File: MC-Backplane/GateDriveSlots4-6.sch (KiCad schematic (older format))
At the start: 3 parts

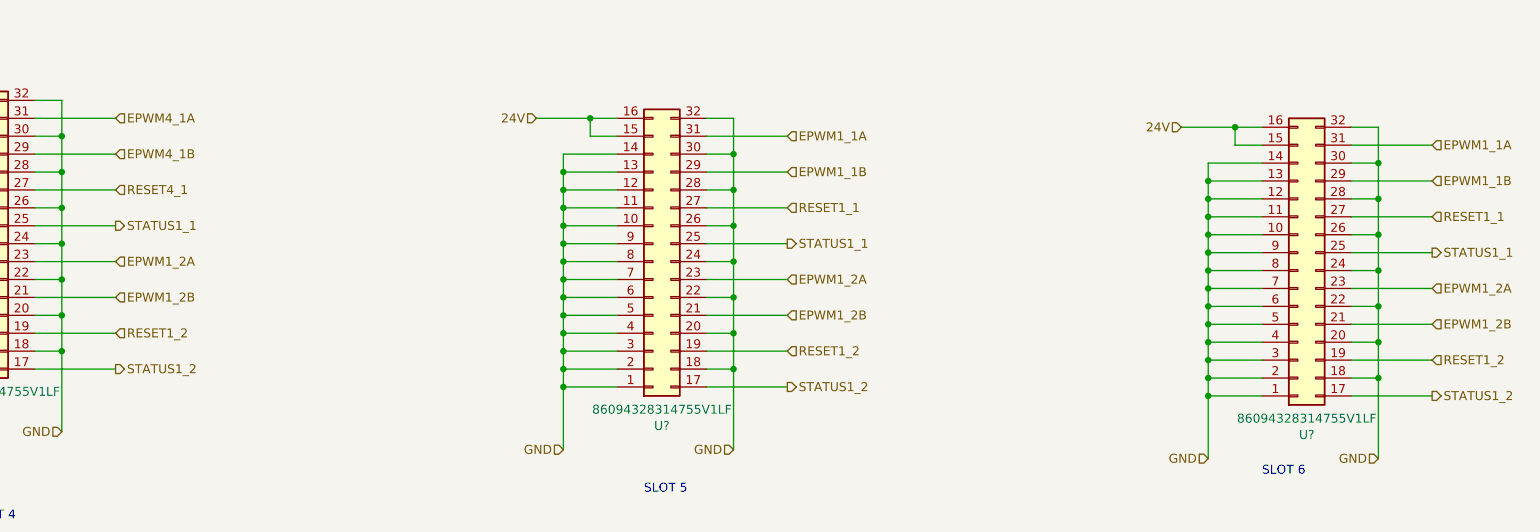
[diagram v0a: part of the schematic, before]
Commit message: added signals for FO slots
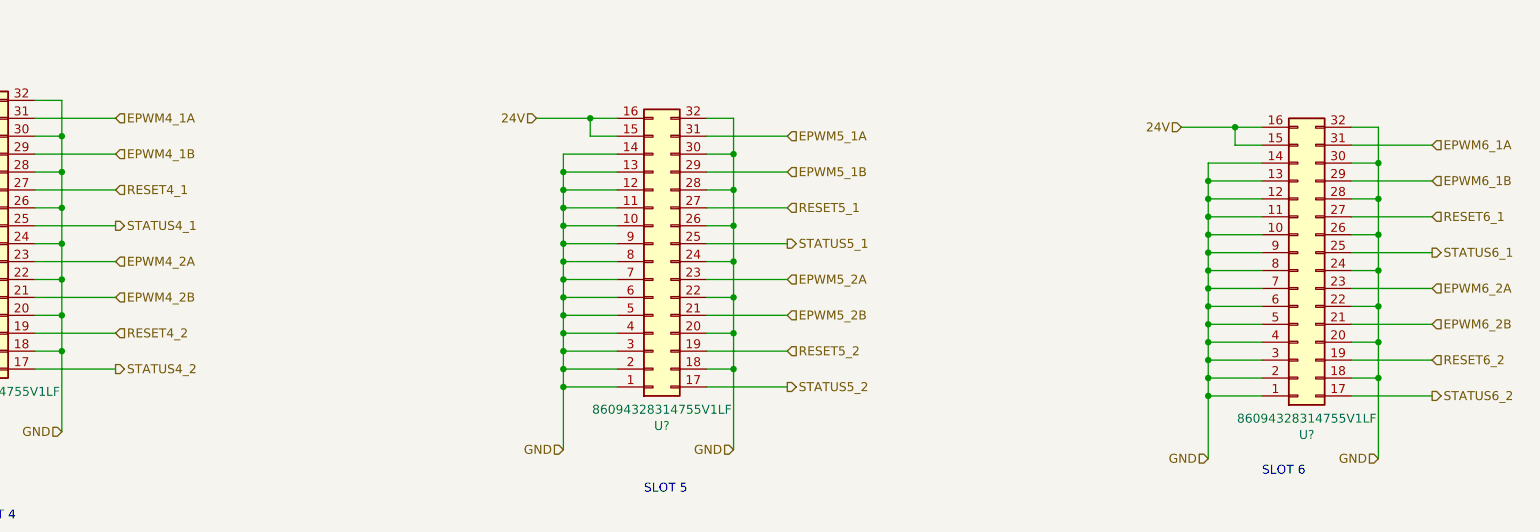
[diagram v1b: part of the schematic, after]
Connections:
- net EPWM1_1A renamed EPWM5_1A
- net EPWM5_1A: no longer U?.31 (Pin_31)
- net EPWM1_1B renamed EPWM5_1B
- net EPWM5_1B: no longer U?.29 (Pin_29)
- removed net EPWM1_2A: U?.23 (Pin_23), U?.23 (Pin_23), U?.23 (Pin_23)
- removed net EPWM1_2B: U?.21 (Pin_21), U?.21 (Pin_21), U?.21 (Pin_21)
- net RESET1_1 renamed RESET5_1
- net RESET5_1: no longer U?.27 (Pin_27)
- removed net RESET1_2: U?.19 (Pin_19), U?.19 (Pin_19), U?.19 (Pin_19)
- removed net STATUS1_1: U?.25 (Pin_25), U?.25 (Pin_25), U?.25 (Pin_25)
- removed net STATUS1_2: U?.17 (Pin_17), U?.17 (Pin_17), U?.17 (Pin_17)
- new net EPWM4_2A: U?.23 (Pin_23)
- new net EPWM4_2B: U?.21 (Pin_21)
- new net EPWM5_2A: U?.23 (Pin_23)
- new net EPWM5_2B: U?.21 (Pin_21)
- new net EPWM6_1A: U?.31 (Pin_31)
- new net EPWM6_1B: U?.29 (Pin_29)
- new net EPWM6_2A: U?.23 (Pin_23)
- new net EPWM6_2B: U?.21 (Pin_21)
- new net RESET4_2: U?.19 (Pin_19)
- new net RESET5_2: U?.19 (Pin_19)
- new net RESET6_1: U?.27 (Pin_27)
- new net RESET6_2: U?.19 (Pin_19)
- new net STATUS4_1: U?.25 (Pin_25)
- new net STATUS4_2: U?.17 (Pin_17)
- new net STATUS5_1: U?.25 (Pin_25)
- new net STATUS5_2: U?.17 (Pin_17)
- new net STATUS6_1: U?.25 (Pin_25)
- new net STATUS6_2: U?.17 (Pin_17)

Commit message: Add files via upload
updating net names and wires
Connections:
- net GND: no longer U?.11 (Pin_11), U?.11 (Pin_11), U?.11 (Pin_11), U?.13 (Pin_13), U?.13 (Pin_13), U?.13 (Pin_13)
- net EPWM4_1A renamed GD_EPWM4_1A
- net EPWM4_1B renamed GD_EPWM4_1B
- net EPWM4_2A renamed GD_EPWM4_2A
- net EPWM4_2B renamed GD_EPWM4_2B
- net EPWM5_1A renamed GD_EPWM5_1A
- net EPWM5_1B renamed GD_EPWM5_1B
- net EPWM5_2A renamed GD_EPWM5_2A
- net EPWM5_2B renamed GD_EPWM5_2B
- net EPWM6_1A renamed GD_EPWM6_1A
- net EPWM6_1B renamed GD_EPWM6_1B
- net EPWM6_2A renamed GD_EPWM6_2A
- net EPWM6_2B renamed GD_EPWM6_2B
- net RESET4_1 renamed GD_RESET4_1
- net RESET4_2 renamed GD_RESET4_2
- net RESET5_1 renamed GD_RESET5_1
- net RESET5_2 renamed GD_RESET5_2
- net RESET6_1 renamed GD_RESET6_1
- net RESET6_2 renamed GD_RESET6_2
- net STATUS4_1 renamed GD_DPWM_STATUS4_1
- net STATUS4_2 renamed GD_DPWM_STATUS4_2
- net STATUS5_1 renamed GD_DPWM_STATUS5_1
- net STATUS5_2 renamed GD_DPWM_STATUS5_2
- net STATUS6_1 renamed GD_DPWM_STATUS6_1
- net STATUS6_2 renamed GD_DPWM_STATUS6_2
- new net EMITTER_ENABLE: U?.13 (Pin_13), U?.13 (Pin_13)
- new net SAFE_STATE_FLAG: U?.11 (Pin_11), U?.11 (Pin_11)
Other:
- note removed: "edit the signal names"
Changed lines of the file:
@@
 $Descr A4 11693 8268
 encoding utf-8
-Sheet 6 7
+Sheet 7 7
 Title ""
 Date ""
@@
 Text Notes 1900 5250 0    50   ~ 0
 SLOT 4
-Text Notes 4650 1300 0    50   ~ 0
-edit the signal names
 $Comp
 L MC-Backplane:86094328314755V1LF U?
@@
 	1750 3100 1450 3100
 Wire Wire Line
-	1450 3100 1450 3200
-Wire Wire Line
-	1750 3200 1450 3200
-Connection ~ 1450 3200
-Wire Wire Line
-	1450 3200 1450 3300
-Wire Wire Line
 	1750 3300 1450 3300
 Connection ~ 1450 3300
-Wire Wire Line
-	1450 3300 1450 3400
-Wire Wire Line
-	1750 3400 1450 3400
-Connection ~ 1450 3400
-Wire Wire Line
-	1450 3400 1450 3500
 Wire Wire Line
 	1750 3500 1450 3500
@@
 GND
 Text HLabel 2700 3000 2    50   Input ~ 0
-EPWM4_1A
+GD_EPWM4_1A
 Wire Wire Line
 	2250 4400 2700 4400
@@
 	2250 4200 2700 4200
 Text HLabel 2700 3200 2    50   Input ~ 0
-EPWM4_1B
+GD_EPWM4_1B
 Text HLabel 2700 3400 2    50   Input ~ 0
-RESET4_1
+GD_RESET4_1
 Text HLabel 2700 3600 2    50   Output ~ 0
-STATUS4_1
+GD_DPWM_STATUS4_1
 Text HLabel 2700 3800 2    50   Input ~ 0
-EPWM4_2A
+GD_EPWM4_2A
 Text HLabel 2700 4000 2    50   Input ~ 0
-EPWM4_2B
+GD_EPWM4_2B
 Text HLabel 2700 4200 2    50   Input ~ 0
-RESET4_2
+GD_RESET4_2
 Text HLabel 2700 4400 2    50   Output ~ 0
-STATUS4_2
+GD_DPWM_STATUS4_2
 Text HLabel 1300 2900 0    50   Input ~ 0
 24V
@@
 24V
 Text HLabel 10050 4550 2    50   Output ~ 0
-STATUS6_2
+GD_DPWM_STATUS6_2
 Text HLabel 10050 4350 2    50   Input ~ 0
-RESET6_2
+GD_RESET6_2
 Text HLabel 10050 4150 2    50   Input ~ 0
-EPWM6_2B
+GD_EPWM6_2B
 Text HLabel 10050 3950 2    50   Input ~ 0
-EPWM6_2A
+GD_EPWM6_2A
 Text HLabel 10050 3750 2    50   Output ~ 0
-STATUS6_1
+GD_DPWM_STATUS6_1
 Text HLabel 10050 3550 2    50   Input ~ 0
-RESET6_1
+GD_RESET6_1
 Text HLabel 10050 3350 2    50   Input ~ 0
-EPWM6_1B
+GD_EPWM6_1B
 Wire Wire Line
 	9600 4350 10050 4350
@@
 	9600 4550 10050 4550
 Text HLabel 10050 3150 2    50   Input ~ 0
-EPWM6_1A
+GD_EPWM6_1A
 Text HLabel 9750 4900 0    50   Input ~ 0
 GND
@@
 Wire Wire Line
 	9100 3650 8800 3650
-Wire Wire Line
-	8800 3550 8800 3650
-Connection ~ 8800 3550
-Wire Wire Line
-	9100 3550 8800 3550
-Wire Wire Line
-	8800 3450 8800 3550
 Connection ~ 8800 3450
 Wire Wire Line
 	9100 3450 8800 3450
-Wire Wire Line
-	8800 3350 8800 3450
-Connection ~ 8800 3350
-Wire Wire Line
-	9100 3350 8800 3350
-Wire Wire Line
-	8800 3250 8800 3350
 Wire Wire Line
 	9100 3250 8800 3250
@@
 24V
 Text HLabel 6450 4500 2    50   Output ~ 0
-STATUS5_2
+GD_DPWM_STATUS5_2
 Text HLabel 6450 4300 2    50   Input ~ 0
-RESET5_2
+GD_RESET5_2
 Text HLabel 6450 4100 2    50   Input ~ 0
-EPWM5_2B
+GD_EPWM5_2B
 Text HLabel 6450 3900 2    50   Input ~ 0
-EPWM5_2A
+GD_EPWM5_2A
 Text HLabel 6450 3700 2    50   Output ~ 0
-STATUS5_1
+GD_DPWM_STATUS5_1
 Text HLabel 6450 3500 2    50   Input ~ 0
-RESET5_1
+GD_RESET5_1
 Text HLabel 6450 3300 2    50   Input ~ 0
-EPWM5_1B
+GD_EPWM5_1B
 Wire Wire Line
 	6000 4300 6450 4300
@@
 	6000 4500 6450 4500
 Text HLabel 6450 3100 2    50   Input ~ 0
-EPWM5_1A
+GD_EPWM5_1A
 Text HLabel 6150 4850 0    50   Input ~ 0
 GND
@@
 Wire Wire Line
 	5500 3600 5200 3600
-Wire Wire Line
-	5200 3500 5200 3600
-Connection ~ 5200 3500
-Wire Wire Line
-	5500 3500 5200 3500
-Wire Wire Line
-	5200 3400 5200 3500
 Connection ~ 5200 3400
 Wire Wire Line
 	5500 3400 5200 3400
-Wire Wire Line
-	5200 3300 5200 3400
-Connection ~ 5200 3300
-Wire Wire Line
-	5500 3300 5200 3300
-Wire Wire Line
-	5200 3200 5200 3300
 Wire Wire Line
 	5500 3200 5200 3200
@@
 Wire Wire Line
 	6000 3100 6450 3100
+Text Notes 9100 5000 0    50   ~ 0
+SLOT 6
+Text Notes 5650 5100 0    50   ~ 0
+SLOT 5
+Wire Wire Line
+	1450 3100 1450 3300
+Wire Wire Line
+	1450 3300 1450 3500
+Wire Wire Line
+	5200 3200 5200 3400
+Wire Wire Line
+	5200 3400 5200 3600
+Wire Wire Line
+	8800 3250 8800 3450
+Wire Wire Line
+	8800 3450 8800 3650
+Text HLabel 1300 3400 0    50   BiDi ~ 0
+SAFE_STATE_FLAG
+Text HLabel 1300 3200 0    50   Input ~ 0
+EMITTER_ENABLE
+Text HLabel 5050 3500 0    50   BiDi ~ 0
+SAFE_STATE_FLAG
+Text HLabel 5050 3300 0    50   Input ~ 0
+EMITTER_ENABLE
+Text HLabel 8650 3550 0    50   BiDi ~ 0
+SAFE_STATE_FLAG
+Text HLabel 8650 3350 0    50   Input ~ 0
+EMITTER_ENABLE
+Wire Wire Line
+	1750 3200 1300 3200
+Wire Wire Line
+	1300 3400 1750 3400
+Wire Wire Line
+	5050 3300 5500 3300
 $Comp
 L MC-Backplane:86094328314755V1LF U?
@@
 	1    0    0    1
 $EndComp
-Text Notes 9100 5000 0    50   ~ 0
-SLOT 6
-Text Notes 5650 5100 0    50   ~ 0
-SLOT 5
+Wire Wire Line
+	5500 3500 5050 3500
 $EndSCHEMATC

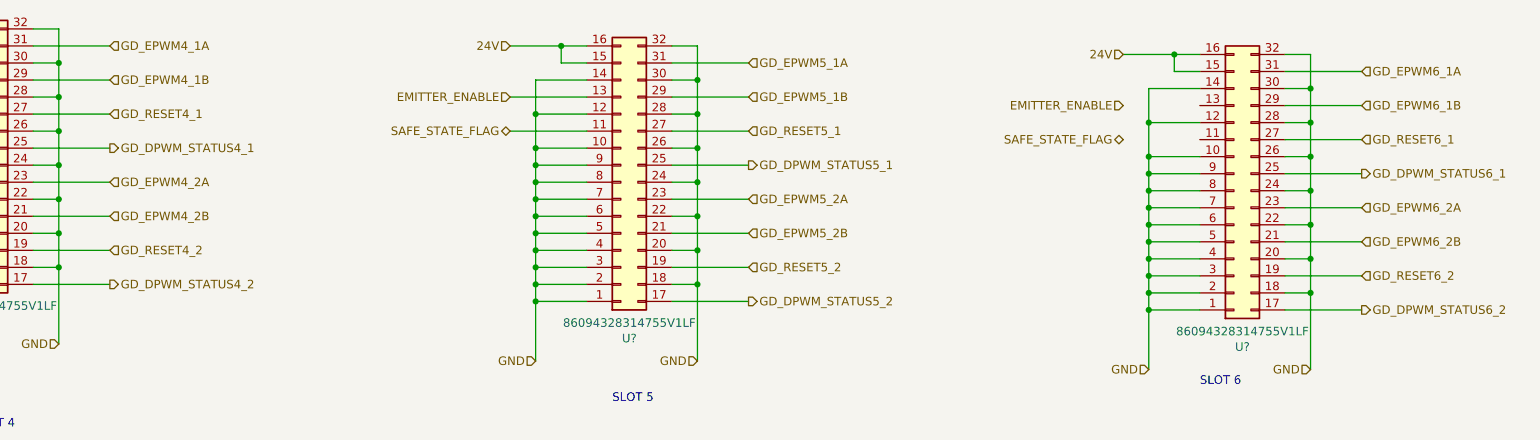
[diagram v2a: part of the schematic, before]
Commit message: Signal naming cleanup/ dsp pin pairing
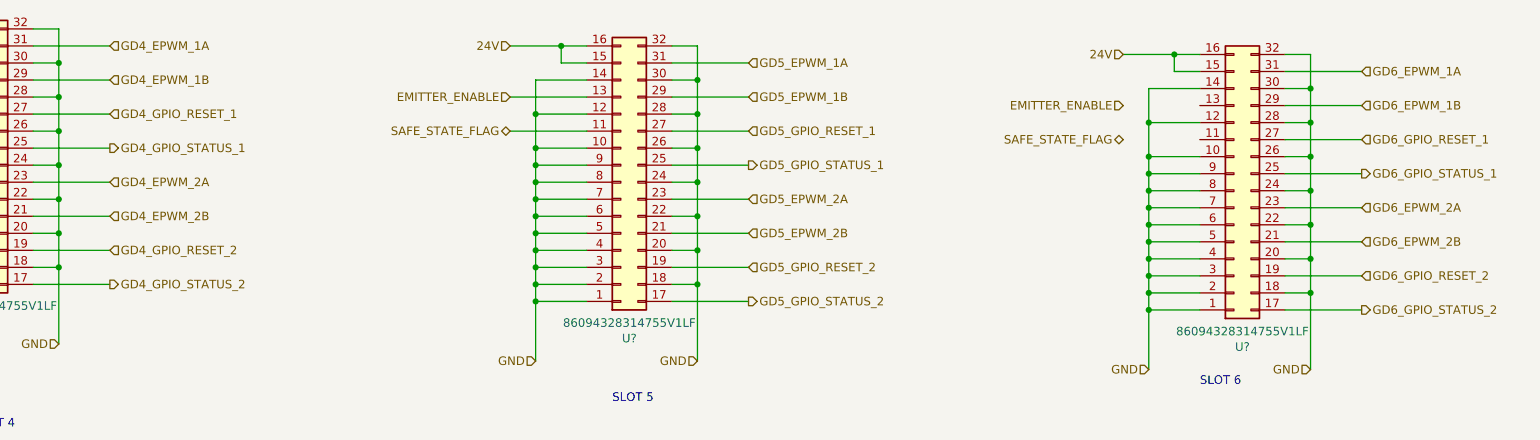
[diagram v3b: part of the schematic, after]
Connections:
- net GD_DPWM_STATUS4_1 renamed GD4_GPIO_STATUS_1
- net GD_DPWM_STATUS4_2 renamed GD4_GPIO_STATUS_2
- net GD_DPWM_STATUS5_1 renamed GD5_GPIO_STATUS_1
- net GD_DPWM_STATUS5_2 renamed GD5_GPIO_STATUS_2
- net GD_DPWM_STATUS6_1 renamed GD6_GPIO_STATUS_1
- net GD_DPWM_STATUS6_2 renamed GD6_GPIO_STATUS_2
- net GD_EPWM4_1A renamed GD4_EPWM_1A
- net GD_EPWM4_1B renamed GD4_EPWM_1B
- net GD_EPWM4_2A renamed GD4_EPWM_2A
- net GD_EPWM4_2B renamed GD4_EPWM_2B
- net GD_EPWM5_1A renamed GD5_EPWM_1A
- net GD_EPWM5_1B renamed GD5_EPWM_1B
- net GD_EPWM5_2A renamed GD5_EPWM_2A
- net GD_EPWM5_2B renamed GD5_EPWM_2B
- net GD_EPWM6_1A renamed GD6_EPWM_1A
- net GD_EPWM6_1B renamed GD6_EPWM_1B
- net GD_EPWM6_2A renamed GD6_EPWM_2A
- net GD_EPWM6_2B renamed GD6_EPWM_2B
- net GD_RESET4_1 renamed GD4_GPIO_RESET_1
- net GD_RESET4_2 renamed GD4_GPIO_RESET_2
- net GD_RESET5_1 renamed GD5_GPIO_RESET_1
- net GD_RESET5_2 renamed GD5_GPIO_RESET_2
- net GD_RESET6_1 renamed GD6_GPIO_RESET_1
- net GD_RESET6_2 renamed GD6_GPIO_RESET_2
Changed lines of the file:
@@
 $Descr A4 11693 8268
 encoding utf-8
-Sheet 7 7
+Sheet 5 7
 Title ""
 Date ""
@@
 GND
 Text HLabel 2700 3000 2    50   Input ~ 0
-GD_EPWM4_1A
+GD4_EPWM_1A
 Wire Wire Line
 	2250 4400 2700 4400
@@
 	2250 4200 2700 4200
 Text HLabel 2700 3200 2    50   Input ~ 0
-GD_EPWM4_1B
+GD4_EPWM_1B
 Text HLabel 2700 3400 2    50   Input ~ 0
-GD_RESET4_1
+GD4_GPIO_RESET_1
 Text HLabel 2700 3600 2    50   Output ~ 0
-GD_DPWM_STATUS4_1
+GD4_GPIO_STATUS_1
 Text HLabel 2700 3800 2    50   Input ~ 0
-GD_EPWM4_2A
+GD4_EPWM_2A
 Text HLabel 2700 4000 2    50   Input ~ 0
-GD_EPWM4_2B
+GD4_EPWM_2B
 Text HLabel 2700 4200 2    50   Input ~ 0
-GD_RESET4_2
+GD4_GPIO_RESET_2
 Text HLabel 2700 4400 2    50   Output ~ 0
-GD_DPWM_STATUS4_2
+GD4_GPIO_STATUS_2
 Text HLabel 1300 2900 0    50   Input ~ 0
 24V
@@
 24V
 Text HLabel 10050 4550 2    50   Output ~ 0
-GD_DPWM_STATUS6_2
+GD6_GPIO_STATUS_2
 Text HLabel 10050 4350 2    50   Input ~ 0
-GD_RESET6_2
+GD6_GPIO_RESET_2
 Text HLabel 10050 4150 2    50   Input ~ 0
-GD_EPWM6_2B
+GD6_EPWM_2B
 Text HLabel 10050 3950 2    50   Input ~ 0
-GD_EPWM6_2A
+GD6_EPWM_2A
 Text HLabel 10050 3750 2    50   Output ~ 0
-GD_DPWM_STATUS6_1
+GD6_GPIO_STATUS_1
 Text HLabel 10050 3550 2    50   Input ~ 0
-GD_RESET6_1
+GD6_GPIO_RESET_1
 Text HLabel 10050 3350 2    50   Input ~ 0
-GD_EPWM6_1B
+GD6_EPWM_1B
 Wire Wire Line
 	9600 4350 10050 4350
@@
 	9600 4550 10050 4550
 Text HLabel 10050 3150 2    50   Input ~ 0
-GD_EPWM6_1A
+GD6_EPWM_1A
 Text HLabel 9750 4900 0    50   Input ~ 0
 GND
@@
 24V
 Text HLabel 6450 4500 2    50   Output ~ 0
-GD_DPWM_STATUS5_2
+GD5_GPIO_STATUS_2
 Text HLabel 6450 4300 2    50   Input ~ 0
-GD_RESET5_2
+GD5_GPIO_RESET_2
 Text HLabel 6450 4100 2    50   Input ~ 0
-GD_EPWM5_2B
+GD5_EPWM_2B
 Text HLabel 6450 3900 2    50   Input ~ 0
-GD_EPWM5_2A
+GD5_EPWM_2A
 Text HLabel 6450 3700 2    50   Output ~ 0
-GD_DPWM_STATUS5_1
+GD5_GPIO_STATUS_1
 Text HLabel 6450 3500 2    50   Input ~ 0
-GD_RESET5_1
+GD5_GPIO_RESET_1
 Text HLabel 6450 3300 2    50   Input ~ 0
-GD_EPWM5_1B
+GD5_EPWM_1B
 Wire Wire Line
 	6000 4300 6450 4300
@@
 	6000 4500 6450 4500
 Text HLabel 6450 3100 2    50   Input ~ 0
-GD_EPWM5_1A
+GD5_EPWM_1A
 Text HLabel 6150 4850 0    50   Input ~ 0
 GND

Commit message: DSP interface pin out
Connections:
- net EMITTER_ENABLE is gone; now on net GND: U?.13 (Pin_13), U?.13 (Pin_13)
- net GD4_GPIO_RESET_2 is gone; now on net GND: U?.19 (Pin_19)
- net GD5_GPIO_RESET_2 is gone; now on net GND: U?.19 (Pin_19)
- net GD5_GPIO_STATUS_2 is gone; now on net CLOCK: U?.17 (Pin_17)
- net GD6_GPIO_RESET_2 is gone; now on net GND: U?.19 (Pin_19)
- net GD6_GPIO_STATUS_1 is gone; now on net GD6_EPWM_1A: U?.25 (Pin_25)
- net GD6_GPIO_STATUS_2 is gone; now on net CLOCK: U?.17 (Pin_17)
- net SAFE_STATE_FLAG is gone; now on net GND: U?.11 (Pin_11), U?.11 (Pin_11)
- net GD6_EPWM_1A: no longer U?.31 (Pin_31)
- net GD6_EPWM_1B: now also U?.23 (Pin_23); no longer U?.29 (Pin_29)
- net GD6_EPWM_2A: now also U?.31 (Pin_31); no longer U?.23 (Pin_23)
- net GD6_EPWM_2B: now also U?.29 (Pin_29); no longer U?.21 (Pin_21)
- net GND: now also U?.11 (Pin_11), U?.13 (Pin_13); no longer U?.2 (Pin_2), U?.2 (Pin_2), U?.2 (Pin_2), U?.4 (Pin_4), U?.4 (Pin_4), U?.4 (Pin_4), U?.6 (Pin_6), U?.6 (Pin_6), U?.6 (Pin_6)
- net GD4_EPWM_1A renamed GD_EPWM_6A
- net GD4_EPWM_1B renamed GD_EPWM_6B
- net GD4_EPWM_2A renamed GD_EPWM_5B
- net GD4_EPWM_2B renamed GD4_GPIO22_STATUS_2
- net GD4_GPIO_RESET_1 renamed GD4_GPIO23_STATUS_1
- net GD4_GPIO_STATUS_1 renamed GD_EPWM_5A
- net GD4_GPIO_STATUS_2 renamed CLOCK
- net GD5_EPWM_1A renamed GD5_EPWM_4A
- net GD5_EPWM_1B renamed GD5_EPWM_4B
- net GD5_EPWM_2A renamed GD5_EPWM_3B
- net GD5_EPWM_2B renamed GD5_GPIO18_STATUS_2
- net GD5_GPIO_RESET_1 renamed GD5_GPIO19_STATUS_1
- net GD5_GPIO_STATUS_1 renamed GD5_EPWM_3A
- net GD6_GPIO_RESET_1 renamed GD6_GPIO16_STATUS_1
- new net GD6_GPIO15_STATUS_2: U?.21 (Pin_21)
- new net GD_GPIO14_RESET: U?.6 (Pin_6), U?.6 (Pin_6), U?.6 (Pin_6)
- new net GPIO12_EMITTER_ENABLE: U?.4 (Pin_4), U?.4 (Pin_4), U?.4 (Pin_4)
- new net GPIO13_SAFE_STATE_FLAG: U?.2 (Pin_2), U?.2 (Pin_2), U?.2 (Pin_2)

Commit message: beginning layout
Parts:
- removed U? (x3): 86094328314755V1LF, symbol MC-Backplane:86094328314755V1LF
- added U16, U17, U18: 86094328314755V1LF, Footprints_MC-Backplane:86094328314755V1LF, symbol Existing_IC_Models:86094328314755V1LF
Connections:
- net 24V: now also U16.A1, U16.A2, U17.A1, U17.A2, U18.A1, U18.A2
- net CLOCK: now also U16.C16, U17.C16, U18.C16
- net GD4_GPIO22_STATUS_2: now also U16.C12
- net GD4_GPIO23_STATUS_1: now also U16.C6
- net GD5_EPWM_3A: now also U17.C8
- net GD5_EPWM_3B: now also U17.C10
- net GD5_EPWM_4A: now also U17.C2
- net GD5_EPWM_4B: now also U17.C4
- net GD5_GPIO18_STATUS_2: now also U17.C12
- net GD5_GPIO19_STATUS_1: now also U17.C6
- net GD6_EPWM_1A: now also U18.C8
- net GD6_EPWM_1B: now also U18.C10
- net GD6_EPWM_2A: now also U18.C2
- net GD6_EPWM_2B: now also U18.C4
- net GD6_GPIO15_STATUS_2: now also U18.C12
- net GD6_GPIO16_STATUS_1: now also U18.C6
- net GD_EPWM_5A: now also U16.C8
- net GD_EPWM_5B: now also U16.C10
- net GD_EPWM_6A: now also U16.C2
- net GD_EPWM_6B: now also U16.C4
- net GD_GPIO14_RESET: now also U16.A11, U17.A11, U18.A11
- net GND: now also U16.A10, U16.A12, U16.A14, U16.A16, U16.A3, U16.A4, U16.A5, U16.A6, U16.A7, U16.A8, U16.A9, U16.B1, U16.B10, U16.B11, U16.B12, U16.B13, U16.B14, U16.B15, U16.B16, U16.B2, U16.B3, U16.B4, U16.B5, U16.B6, U16.B7, U16.B8, U16.B9, U16.C1, U16.C11, U16.C13, U16.C14, U16.C15, U16.C3, U16.C5, U16.C7, U16.C9, U17.A10, U17.A12, U17.A14, U17.A16, U17.A3, U17.A4, U17.A5, U17.A6, U17.A7, U17.A8, U17.A9, U17.B1, U17.B10, U17.B11, U17.B12, U17.B13, U17.B14, U17.B15, U17.B16, U17.B2, U17.B3, U17.B4, U17.B5, U17.B6, U17.B7, U17.B8, U17.B9, U17.C1, U17.C11, U17.C13, U17.C14, U17.C15, U17.C3, U17.C5, U17.C7, U17.C9, U18.A10, U18.A12, U18.A14, U18.A16, U18.A3, U18.A4, U18.A5, U18.A6, U18.A7, U18.A8, U18.A9, U18.B1, U18.B10, U18.B11, U18.B12, U18.B13, U18.B14, U18.B15, U18.B16, U18.B2, U18.B3, U18.B4, U18.B5, U18.B6, U18.B7, U18.B8, U18.B9, U18.C1, U18.C11, U18.C13, U18.C14, U18.C15, U18.C3, U18.C5, U18.C7, U18.C9
- net GPIO12_EMITTER_ENABLE: now also U16.A13, U17.A13, U18.A13
- net GPIO13_SAFE_STATE_FLAG: now also U16.A15, U17.A15, U18.A15
